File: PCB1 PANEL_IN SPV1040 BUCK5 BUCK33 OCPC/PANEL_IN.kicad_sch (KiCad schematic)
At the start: 5 parts

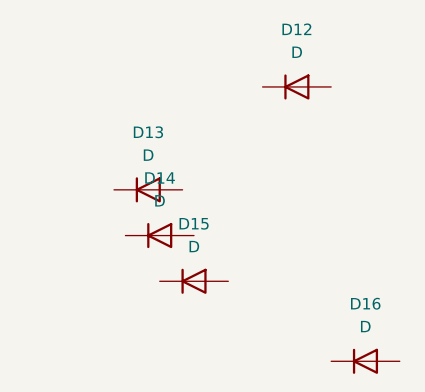
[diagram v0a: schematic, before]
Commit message: Relabeling according to standards
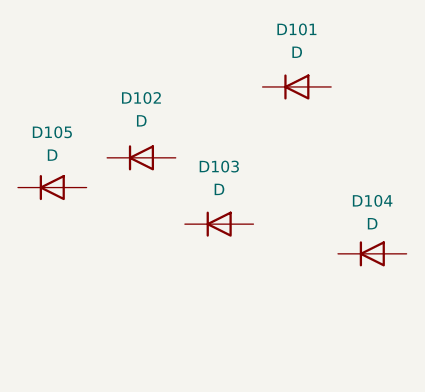
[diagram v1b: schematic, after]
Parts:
- renumbered D12 to D101, D14 to D102, D15 to D103, D16 to D104, D13 to D105
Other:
- moved on the sheet: D102, D103, D104, D105
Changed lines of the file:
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@@
 	(symbol
 		(lib_id "Device:D")
-		(at 95.25 92.71 0)
+		(at 84.582 92.456 0)
 		(unit 1)
 		(exclude_from_sim no)
@@
 		(dnp no)
 		(fields_autoplaced yes)
-		(property "Reference" "D13"
-			(at 95.25 86.36 0)
+		(property "Reference" "D105"
+			(at 84.582 86.36 0)
 			(effects
 				(font
@@
 		)
 		(property "Value" "D"
-			(at 95.25 88.9 0)
+			(at 84.582 88.9 0)
 			(effects
 				(font
@@
 		)
 		(property "Footprint" ""
-			(at 95.25 92.71 0)
+			(at 84.582 92.456 0)
 			(effects
 				(font
@@
 		)
 		(property "Datasheet" "~"
-			(at 95.25 92.71 0)
+			(at 84.582 92.456 0)
 			(effects
 				(font
@@
 		)
 		(property "Description" "Diode"
-			(at 95.25 92.71 0)
+			(at 84.582 92.456 0)
 			(effects
 				(font
@@
 		)
 		(property "Sim.Device" "D"
-			(at 95.25 92.71 0)
+			(at 84.582 92.456 0)
 			(effects
 				(font
@@
 		)
 		(property "Sim.Pins" "1=K 2=A"
-			(at 95.25 92.71 0)
+			(at 84.582 92.456 0)
 			(effects
 				(font
@@
 			(project "PCB1 PANEL_IN SPV1040 BUCK5 BUCK33 OCPC"
 				(path "/494c9d9f-6b33-4248-a813-27ffaaa929bd/e761ae96-2f77-47a8-a4f2-e723b65c98c7"
-					(reference "D13")
+					(reference "D105")
 					(unit 1)
 				)
@@
 	(symbol
 		(lib_id "Device:D")
-		(at 96.52 97.79 0)
+		(at 94.488 89.154 0)
 		(unit 1)
 		(exclude_from_sim no)
@@
 		(dnp no)
 		(fields_autoplaced yes)
-		(property "Reference" "D14"
-			(at 96.52 91.44 0)
+		(property "Reference" "D102"
+			(at 94.488 82.55 0)
 			(effects
 				(font
@@
 		)
 		(property "Value" "D"
-			(at 96.52 93.98 0)
+			(at 94.488 85.09 0)
 			(effects
 				(font
@@
 		)
 		(property "Footprint" ""
-			(at 96.52 97.79 0)
+			(at 94.488 89.154 0)
 			(effects
 				(font
@@
 		)
 		(property "Datasheet" "~"
-			(at 96.52 97.79 0)
+			(at 94.488 89.154 0)
 			(effects
 				(font
@@
 		)
 		(property "Description" "Diode"
-			(at 96.52 97.79 0)
+			(at 94.488 89.154 0)
 			(effects
 				(font
@@
 		)
 		(property "Sim.Device" "D"
-			(at 96.52 97.79 0)
+			(at 94.488 89.154 0)
 			(effects
 				(font
@@
 		)
 		(property "Sim.Pins" "1=K 2=A"
-			(at 96.52 97.79 0)
+			(at 94.488 89.154 0)
 			(effects
 				(font
@@
 			(project "PCB1 PANEL_IN SPV1040 BUCK5 BUCK33 OCPC"
 				(path "/494c9d9f-6b33-4248-a813-27ffaaa929bd/e761ae96-2f77-47a8-a4f2-e723b65c98c7"
-					(reference "D14")
+					(reference "D102")
 					(unit 1)
 				)
@@
 	(symbol
 		(lib_id "Device:D")
-		(at 119.38 111.76 0)
+		(at 120.142 99.822 0)
 		(unit 1)
 		(exclude_from_sim no)
@@
 		(dnp no)
 		(fields_autoplaced yes)
-		(property "Reference" "D16"
-			(at 119.38 105.41 0)
+		(property "Reference" "D104"
+			(at 120.142 93.98 0)
 			(effects
 				(font
@@
 		)
 		(property "Value" "D"
-			(at 119.38 107.95 0)
+			(at 120.142 96.52 0)
 			(effects
 				(font
@@
 		)
 		(property "Footprint" ""
-			(at 119.38 111.76 0)
+			(at 120.142 99.822 0)
 			(effects
 				(font
@@
 		)
 		(property "Datasheet" "~"
-			(at 119.38 111.76 0)
+			(at 120.142 99.822 0)
 			(effects
 				(font
@@
 		)
 		(property "Description" "Diode"
-			(at 119.38 111.76 0)
+			(at 120.142 99.822 0)
 			(effects
 				(font
@@
 		)
 		(property "Sim.Device" "D"
-			(at 119.38 111.76 0)
+			(at 120.142 99.822 0)
 			(effects
 				(font
@@
 		)
 		(property "Sim.Pins" "1=K 2=A"
-			(at 119.38 111.76 0)
+			(at 120.142 99.822 0)
 			(effects
 				(font
@@
 			(project "PCB1 PANEL_IN SPV1040 BUCK5 BUCK33 OCPC"
 				(path "/494c9d9f-6b33-4248-a813-27ffaaa929bd/e761ae96-2f77-47a8-a4f2-e723b65c98c7"
-					(reference "D16")
+					(reference "D104")
 					(unit 1)
 				)
@@
 	(symbol
 		(lib_id "Device:D")
-		(at 100.33 102.87 0)
+		(at 103.124 96.52 0)
 		(unit 1)
 		(exclude_from_sim no)
@@
 		(dnp no)
 		(fields_autoplaced yes)
-		(property "Reference" "D15"
-			(at 100.33 96.52 0)
+		(property "Reference" "D103"
+			(at 103.124 90.17 0)
 			(effects
 				(font
@@
 		)
 		(property "Value" "D"
-			(at 100.33 99.06 0)
+			(at 103.124 92.71 0)
 			(effects
 				(font
@@
 		)
 		(property "Footprint" ""
-			(at 100.33 102.87 0)
+			(at 103.124 96.52 0)
 			(effects
 				(font
@@
 		)
 		(property "Datasheet" "~"
-			(at 100.33 102.87 0)
+			(at 103.124 96.52 0)
 			(effects
 				(font
@@
 		)
 		(property "Description" "Diode"
-			(at 100.33 102.87 0)
+			(at 103.124 96.52 0)
 			(effects
 				(font
@@
 		)
 		(property "Sim.Device" "D"
-			(at 100.33 102.87 0)
+			(at 103.124 96.52 0)
 			(effects
 				(font
@@
 		)
 		(property "Sim.Pins" "1=K 2=A"
-			(at 100.33 102.87 0)
+			(at 103.124 96.52 0)
 			(effects
 				(font
@@
 			(project "PCB1 PANEL_IN SPV1040 BUCK5 BUCK33 OCPC"
 				(path "/494c9d9f-6b33-4248-a813-27ffaaa929bd/e761ae96-2f77-47a8-a4f2-e723b65c98c7"
-					(reference "D15")
+					(reference "D103")
 					(unit 1)
 				)
@@
 		(dnp no)
 		(fields_autoplaced yes)
-		(property "Reference" "D12"
+		(property "Reference" "D101"
 			(at 111.76 74.93 0)
 			(effects
@@
 			(project "PCB1 PANEL_IN SPV1040 BUCK5 BUCK33 OCPC"
 				(path "/494c9d9f-6b33-4248-a813-27ffaaa929bd/e761ae96-2f77-47a8-a4f2-e723b65c98c7"
-					(reference "D12")
+					(reference "D101")
 					(unit 1)
 				)
